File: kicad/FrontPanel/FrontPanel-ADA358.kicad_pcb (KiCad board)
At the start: 2 copper layers, 198 x 58 mm, 18 parts

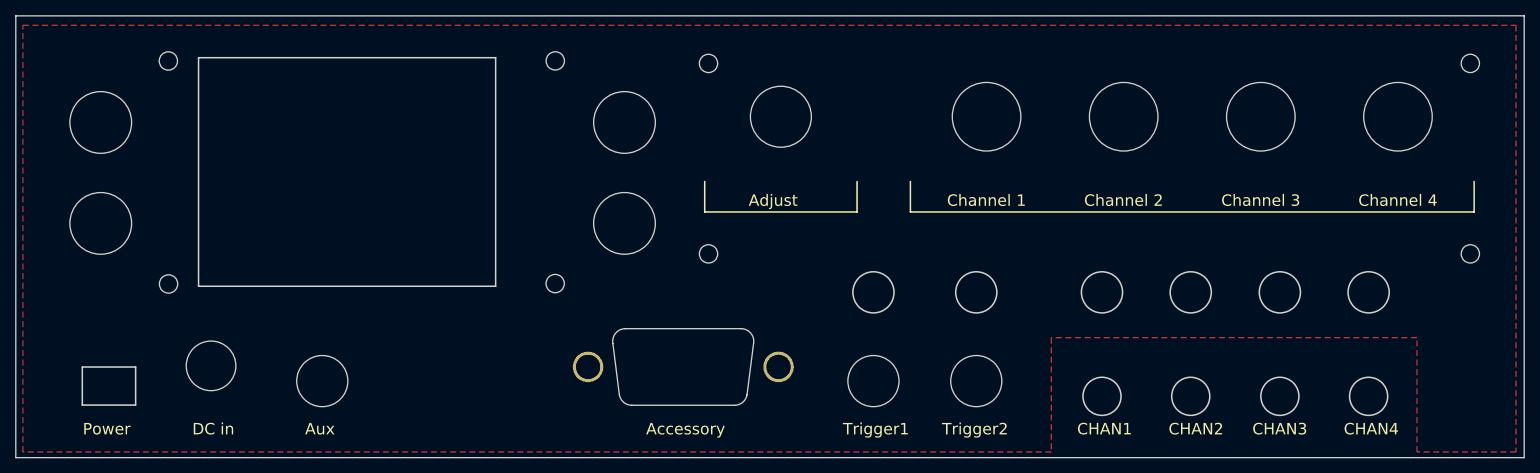
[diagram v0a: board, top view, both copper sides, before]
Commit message: FrontPanel MainBoard alignment
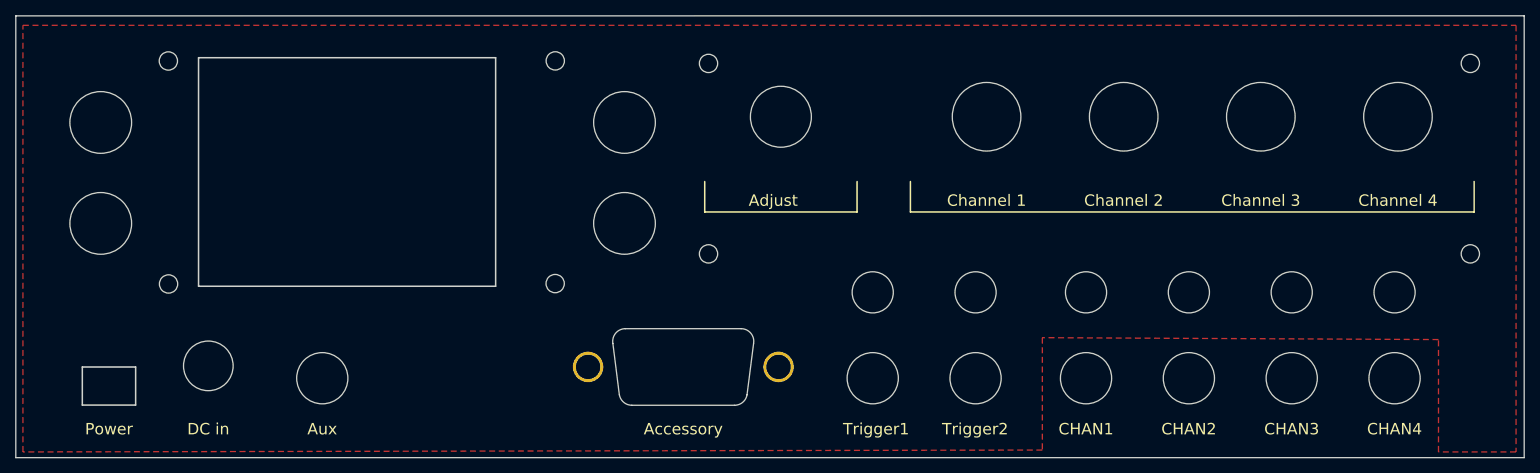
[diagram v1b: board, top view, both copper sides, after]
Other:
- outline, holes or cut-outs redrawn
- board text added: "ZC95 Front panel v0.4-m"
- board text removed: "ZC95 Front panel v0.3"
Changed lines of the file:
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@@
 		(solder_mask_min_width 0.25)
 		(allow_soldermask_bridges_in_footprints no)
+		(grid_origin 24.07 143.75)
 		(pcbplotparams
 			(layerselection 0x00010fc_ffffffff)
@@
 		(layer "F.SilkS")
 	)
-	(gr_circle
-		(center 136.65 133.7)
-		(end 138.25 136.65)
-		(stroke
-			(width 0.15)
-			(type solid)
-		)
-		(fill none)
-		(layer "Edge.Cuts")
-	)
-	(gr_circle
-		(center 64.3 133.7)
-		(end 65.9 136.65)
-		(stroke
-			(width 0.15)
-			(type solid)
-		)
-		(fill none)
-		(layer "Edge.Cuts")
-	)
 	(gr_line
 		(start 48.057 121.25)
@@
 		(layer "Edge.Cuts")
 	)
-	(gr_circle
-		(center 190 135.7)
-		(end 191.5 137.7)
-		(stroke
-			(width 0.2)
-			(type solid)
-		)
-		(fill none)
-		(layer "Edge.Cuts")
-	)
 	(gr_line
 		(start 48.057 91.25)
@@
 		(layer "Edge.Cuts")
 	)
-	(gr_circle
-		(center 201.65 135.7)
-		(end 203.15 137.7)
-		(stroke
-			(width 0.2)
-			(type solid)
-		)
-		(fill none)
-		(layer "Edge.Cuts")
-	)
 	(gr_line
 		(start 24.07 85.76)
@@
 		(layer "Edge.Cuts")
 	)
-	(gr_circle
-		(center 166.65 135.7)
-		(end 168.15 137.7)
-		(stroke
-			(width 0.2)
-			(type solid)
-		)
-		(fill none)
-		(layer "Edge.Cuts")
-	)
-	(gr_circle
-		(center 178.3 122.05)
-		(end 181 122.05)
-		(stroke
-			(width 0.2)
-			(type solid)
-		)
-		(fill none)
-		(layer "Edge.Cuts")
-	)
-	(gr_circle
-		(center 190 122.05)
-		(end 192.7 122.05)
-		(stroke
-			(width 0.2)
-			(type solid)
-		)
-		(fill none)
-		(layer "Edge.Cuts")
-	)
-	(gr_circle
-		(center 201.65 122.05)
-		(end 204.35 122.05)
-		(stroke
-			(width 0.2)
-			(type solid)
-		)
-		(fill none)
-		(layer "Edge.Cuts")
-	)
-	(gr_circle
-		(center 150.15 122.05)
-		(end 152.85 122.05)
-		(stroke
-			(width 0.2)
-			(type solid)
-		)
-		(fill none)
-		(layer "Edge.Cuts")
-	)
-	(gr_circle
-		(center 136.65 122.05)
-		(end 139.35 122.05)
-		(stroke
-			(width 0.2)
-			(type solid)
-		)
-		(fill none)
-		(layer "Edge.Cuts")
-	)
-	(gr_circle
-		(center 150.15 133.7)
-		(end 151.75 136.65)
-		(stroke
-			(width 0.15)
-			(type solid)
-		)
-		(fill none)
-		(layer "Edge.Cuts")
-	)
 	(gr_line
 		(start 39.8 131.85)
@@
 	)
 	(gr_circle
-		(center 49.7 131.7)
-		(end 52.9 132.3)
-		(stroke
-			(width 0.15)
+		(center 150.054673 133.323162)
+		(end 146.694673 133.323162)
+		(stroke
+			(width 0.16)
+			(type solid)
+		)
+		(fill none)
+		(layer "Edge.Cuts")
+	)
+	(gr_circle
+		(center 178.054673 122.05)
+		(end 175.354673 122.05)
+		(stroke
+			(width 0.16)
+			(type solid)
+		)
+		(fill none)
+		(layer "Edge.Cuts")
+	)
+	(gr_circle
+		(center 49.34042 131.7)
+		(end 46.084656 131.7)
+		(stroke
+			(width 0.16)
+			(type solid)
+		)
+		(fill none)
+		(layer "Edge.Cuts")
+	)
+	(gr_circle
+		(center 64.3 133.323162)
+		(end 60.94 133.323162)
+		(stroke
+			(width 0.16)
 			(type solid)
 		)
@@
 		(layer "Edge.Cuts")
 	)
+	(gr_circle
+		(center 191.554673 133.323162)
+		(end 188.194673 133.323162)
+		(stroke
+			(width 0.16)
+			(type solid)
+		)
+		(fill none)
+		(layer "Edge.Cuts")
+	)
 	(gr_line
 		(start 32.8 136.85)
@@
 		(layer "Edge.Cuts")
 	)
+	(gr_circle
+		(center 191.554673 122.05)
+		(end 188.854673 122.05)
+		(stroke
+			(width 0.16)
+			(type solid)
+		)
+		(fill none)
+		(layer "Edge.Cuts")
+	)
+	(gr_circle
+		(center 178.054673 133.323162)
+		(end 174.694673 133.323162)
+		(stroke
+			(width 0.16)
+			(type solid)
+		)
+		(fill none)
+		(layer "Edge.Cuts")
+	)
+	(gr_circle
+		(center 136.554673 122.05)
+		(end 133.854673 122.05)
+		(stroke
+			(width 0.16)
+			(type solid)
+		)
+		(fill none)
+		(layer "Edge.Cuts")
+	)
 	(gr_line
 		(start 32.8 131.85)
@@
 	)
 	(gr_circle
-		(center 166.65 122.05)
-		(end 169.35 122.05)
-		(stroke
-			(width 0.2)
+		(center 164.554673 122.05)
+		(end 161.854673 122.05)
+		(stroke
+			(width 0.16)
 			(type solid)
 		)
@@
 	)
 	(gr_circle
-		(center 178.3 135.7)
-		(end 179.8 137.7)
-		(stroke
-			(width 0.2)
+		(center 150.054673 122.05)
+		(end 147.354673 122.05)
+		(stroke
+			(width 0.16)
+			(type solid)
+		)
+		(fill none)
+		(layer "Edge.Cuts")
+	)
+	(gr_circle
+		(center 205.054673 122.05)
+		(end 202.354673 122.05)
+		(stroke
+			(width 0.16)
+			(type solid)
+		)
+		(fill none)
+		(layer "Edge.Cuts")
+	)
+	(gr_circle
+		(center 136.554673 133.323162)
+		(end 133.194673 133.323162)
+		(stroke
+			(width 0.16)
+			(type solid)
+		)
+		(fill none)
+		(layer "Edge.Cuts")
+	)
+	(gr_circle
+		(center 205.054673 133.323162)
+		(end 201.694673 133.323162)
+		(stroke
+			(width 0.16)
+			(type solid)
+		)
+		(fill none)
+		(layer "Edge.Cuts")
+	)
+	(gr_circle
+		(center 164.554673 133.323162)
+		(end 161.194673 133.323162)
+		(stroke
+			(width 0.16)
 			(type solid)
 		)
@@
 		)
 	)
-	(gr_text "ZC95 \nFront panel\nv0.3"
+	(gr_text "ZC95 \nFront panel\nv0.4-m"
 		(at 157 116.5 0)
 		(layer "B.SilkS")
@@
 	)
 	(gr_text "CHAN2"
-		(at 179 140 0)
+		(at 178.054673 140 0)
 		(layer "F.SilkS")
 		(effects
@@
 	)
 	(gr_text "CHAN3"
-		(at 190 140 0)
+		(at 191.554673 140 0)
 		(layer "F.SilkS")
 		(effects
@@
 	)
 	(gr_text "CHAN4"
-		(at 202 140 0)
+		(at 205.054673 140 0)
 		(layer "F.SilkS")
 		(effects
@@
 	)
 	(gr_text "CHAN1"
-		(at 167 140 0)
+		(at 164.554673 140 0)
 		(layer "F.SilkS")
 		(effects
@@
 	)
 	(gr_text "Accessory"
-		(at 112 140 0)
+		(at 111.69 140 0)
 		(layer "F.SilkS")
 		(effects
@@
 	)
 	(gr_text "Power"
-		(at 36 140 0)
+		(at 36.3 140 0)
 		(layer "F.SilkS")
 		(effects
@@
 	)
 	(gr_text "DC in"
-		(at 50 140 0)
+		(at 49.34042 140 0)
 		(layer "F.SilkS")
 		(effects
@@
 	)
 	(gr_text "Aux"
-		(at 64 140 0)
+		(at 64.3 140 0)
 		(layer "F.SilkS")
 		(effects
@@
 		(polygon
 			(pts
-				(xy 25 87) (xy 221 87) (xy 221 143) (xy 208 143) (xy 208 128) (xy 160 128) (xy 160 143) (xy 25 143)
-			)
-		)
+				(xy 25 87) (xy 221 87) (xy 221 143) (xy 210.82 143) (xy 210.82 128.25) (xy 158.82 128) (xy 158.82 142.75)
+				(xy 25 143)
+			)
+		)

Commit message: Move to fit new 3.5mm holes
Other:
- board text added: "ZC95 Front panel v0.4-3.5mm"
- board text removed: "ZC95 Front panel v0.4-m"
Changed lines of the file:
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@@
 		)
 	)
-	(gr_text "ZC95 \nFront panel\nv0.4-m"
-		(at 157 116.5 0)
+	(gr_text "ZC95 \nFront panel\nv0.4-3.5mm"
+		(at 156.82 114.75 0)
 		(layer "B.SilkS")
 		(effects
